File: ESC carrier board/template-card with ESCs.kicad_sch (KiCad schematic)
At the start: 13 parts, among them J1 Conn_01x10_Pin, J3 Conn_01x04_Pin, J4 Conn_01x04_Pin, J5 Conn_01x04_Pin, SW1 SW_DPDT_x2, U2 ESC, U4 ESC, U6 ESC

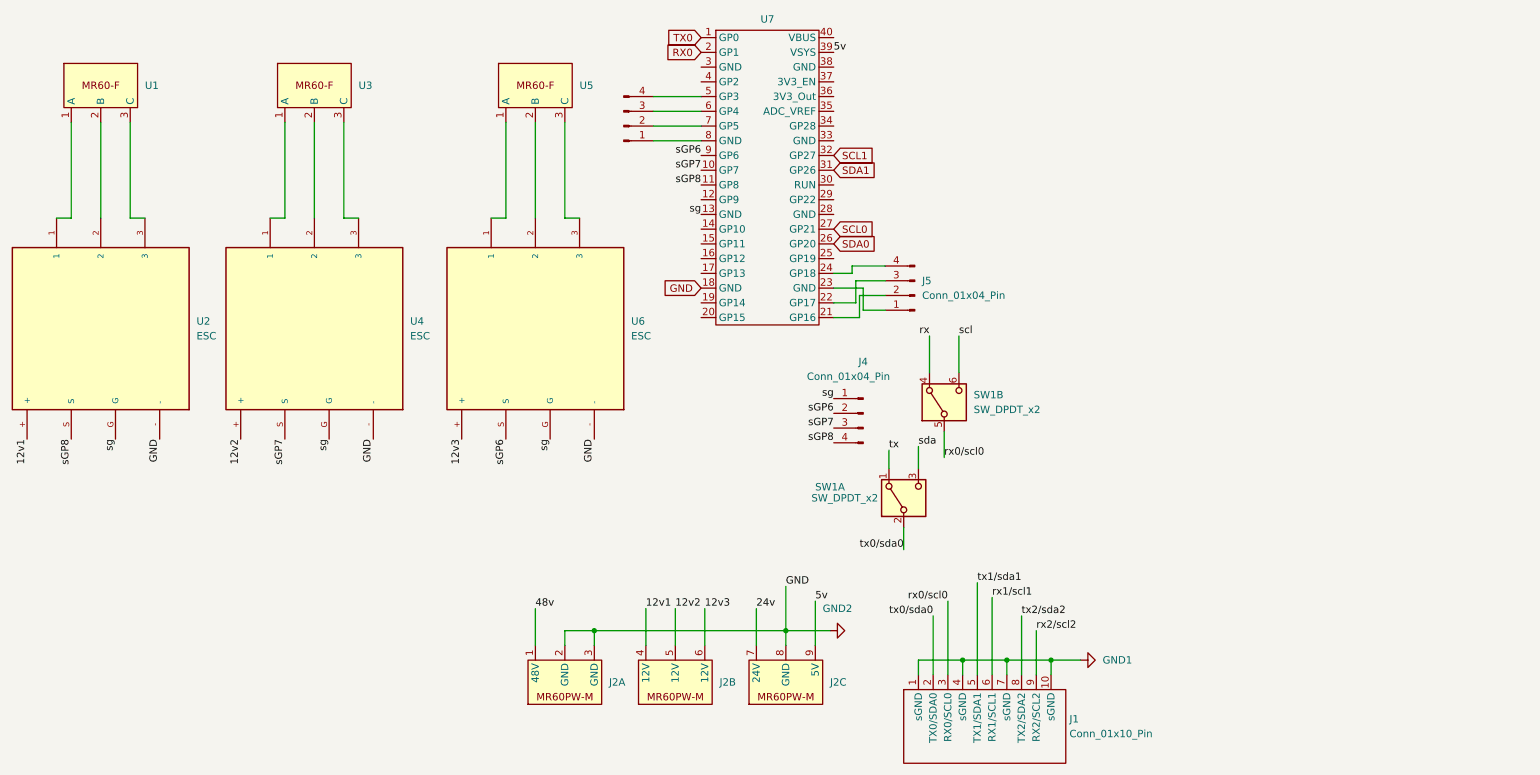
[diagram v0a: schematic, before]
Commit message: Routed board
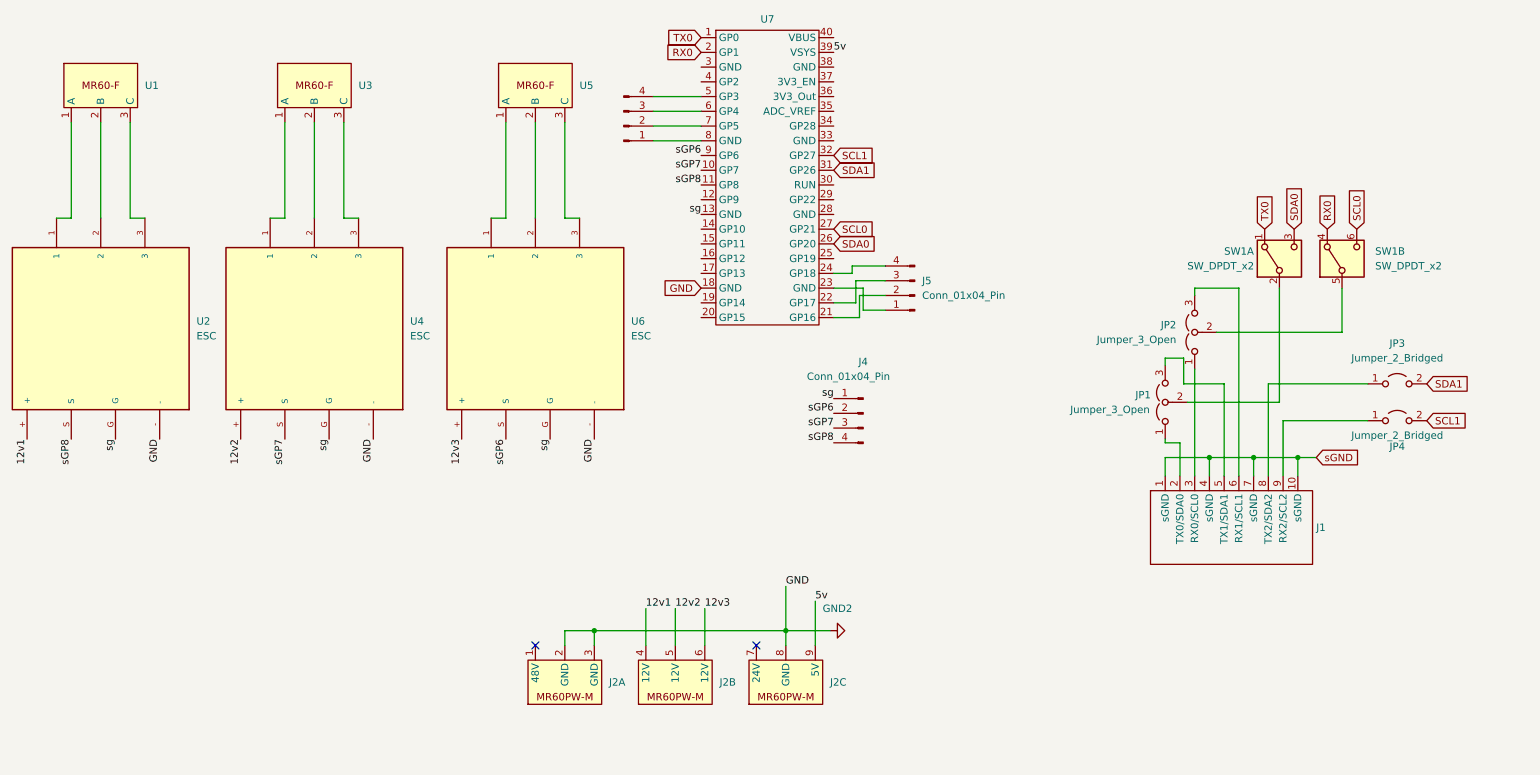
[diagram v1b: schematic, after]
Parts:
- added JP1, JP2: Jumper_3_Open, Jumper:SolderJumper-3_P1.3mm_Open_RoundedPad1.0x1.5mm, symbol Jumper:Jumper_3_Open
- added JP3, JP4: Jumper_2_Bridged, Jumper:SolderJumper-2_P1.3mm_Open_RoundedPad1.0x1.5mm, symbol Jumper:Jumper_2_Open
- J1: value Conn_01x10_Pin -> ~
- SW1: footprint 2024-backplane:SW_CUI_DPDT -> Kelpie_Default:CUI-Switch-SMD
- U1, U3, U5: footprint ESC-Thruster:MR60-F -> 2024-backplane:MR60-F
- U7: footprint ESC-carrier:ESP32-S3-Pico -> Kelpie_Default:ESP32-S3-Pico
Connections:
- net rx is gone; now on net RX0: SW1.4 (A)
- net scl is gone; now on net SCL0: SW1.6 (C)
- net sda is gone; now on net SDA0: SW1.3 (C)
- net tx is gone; now on net TX0: SW1.1 (A)
- net SCL1: now also JP4.2 (B)
- net SDA1: now also JP3.2 (B)
- net 24v: no longer names the net of J2.7 (24V)
- net 48v: no longer names the net of J2.1 (48V)
- net GND1 renamed sGND
- net rx0/scl0: no longer names the net of J1.3 (RX0/SCL0)
- net rx0/scl0: now also JP2.1 (A); no longer SW1.5 (B)
- net rx1/scl1: no longer names the net of J1.6 (RX1/SCL1)
- net rx1/scl1: now also JP2.3 (B)
- net rx2/scl2: no longer names the net of J1.9 (RX2/SCL2)
- net rx2/scl2: now also JP4.1 (A)
- net tx0/sda0: no longer names the net of J1.2 (TX0/SDA0)
- net tx0/sda0: now also JP1.1 (A); no longer SW1.2 (B)
- net tx1/sda1: no longer names the net of J1.5 (TX1/SDA1)
- net tx1/sda1: now also JP1.3 (B)
- net tx2/sda2: no longer names the net of J1.8 (TX2/SDA2)
- net tx2/sda2: now also JP3.1 (A)
- new net: JP2.2 (C), SW1.5 (B)
- new net: JP1.2 (C), SW1.2 (B)
- no-connect marks 0 -> 2

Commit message: Modified board and footprints
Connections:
- net sg is gone; now on net sGND: J4.1 (Pin_1), U2.G, U4.G, U6.G, U7.13 (GND)
- net GND2: now also J2.10 (Mount)
- net sGND: now also J3.1 (Pin_1), J5.1 (Pin_1), U7.23 (GND), U7.28 (GND), U7.3 (GND), U7.33 (GND), U7.38 (GND), U7.8 (GND)
- no-connect marks 2 -> 18
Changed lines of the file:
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@@
   (junction (at 236.855 89.535) (diameter 0) (color 0 0 0 0)
   )
+  (junction (at 172.085 64.135) (diameter 0) (color 0 0 0 0)
+  )
+  (junction (at 134.62 34.925) (diameter 0) (color 0 0 0 0)
+  )
   (junction (at 244.475 89.535) (diameter 0) (color 0 0 0 0)
   )
   (junction (at 156.21 119.38) (diameter 0) (color 0 0 0 0)
   )
+  (junction (at 139.7 47.625) (diameter 0) (color 0 0 0 0)
+  )
   (junction (at 123.19 119.38) (diameter 0) (color 0 0 0 0)
   )
   (junction (at 229.235 89.535) (diameter 0) (color 0 0 0 0)
   )
+  (no_connect (at 164.465 29.845))
+  (no_connect (at 141.605 57.785))
+  (no_connect (at 141.605 55.245))
+  (no_connect (at 164.465 55.245))
   (no_connect (at 151.13 121.92))
+  (no_connect (at 164.465 42.545))
+  (no_connect (at 164.465 17.145))
+  (no_connect (at 141.605 65.405))
+  (no_connect (at 164.465 27.305))
+  (no_connect (at 164.465 32.385))
+  (no_connect (at 164.465 45.085))
+  (no_connect (at 141.605 45.085))
+  (no_connect (at 164.465 24.765))
+  (no_connect (at 141.605 52.705))
+  (no_connect (at 141.605 62.865))
+  (no_connect (at 141.605 24.765))
   (no_connect (at 113.03 121.92))
+  (no_connect (at 141.605 50.165))
   (wire (pts (xy 80.01 48.26) (xy 80.01 31.75))
     (stroke (width 0) (type default))
   )
+  (wire (pts (xy 106.68 132.715) (xy 106.68 129.54))
+    (stroke (width 0) (type default))
+  )
   (wire (pts (xy 43.18 31.75) (xy 43.18 48.26))
     (stroke (width 0) (type default))
@@
     (stroke (width 0) (type default))
   )
+  (wire (pts (xy 139.7 47.625) (xy 139.7 50.165))
+    (stroke (width 0) (type default))
+  )
   (wire (pts (xy 167.64 57.785) (xy 167.64 56.515))
     (stroke (width 0) (type default))
@@
     (stroke (width 0) (type default))
   )
+  (wire (pts (xy 134.62 37.465) (xy 133.35 37.465))
+    (stroke (width 0) (type default))
+  )
   (wire (pts (xy 156.21 111.76) (xy 156.21 119.38))
     (stroke (width 0) (type default))
@@
     (stroke (width 0) (type default))
   )
+  (wire (pts (xy 139.7 47.625) (xy 141.605 47.625))
+    (stroke (width 0) (type default))
+  )
   (wire (pts (xy 133.35 29.845) (xy 141.605 29.845))
     (stroke (width 0) (type default))
@@
     (stroke (width 0) (type default))
   )
-  (wire (pts (xy 133.35 34.925) (xy 141.605 34.925))
+  (wire (pts (xy 133.35 34.925) (xy 134.62 34.925))
     (stroke (width 0) (type default))
   )
@@
     (stroke (width 0) (type default))
   )
+  (wire (pts (xy 106.68 129.54) (xy 109.22 129.54))
+    (stroke (width 0) (type default))
+  )
   (wire (pts (xy 241.935 83.185) (xy 256.54 83.185))
     (stroke (width 0) (type default))
@@
     (stroke (width 0) (type default))
   )
+  (wire (pts (xy 134.62 34.925) (xy 134.62 37.465))
+    (stroke (width 0) (type default))
+  )
   (wire (pts (xy 224.155 86.995) (xy 224.155 92.71))
     (stroke (width 0) (type default))
@@
     (stroke (width 0) (type default))
   )
+  (wire (pts (xy 172.085 64.135) (xy 172.085 67.31))
+    (stroke (width 0) (type default))
+  )
+  (wire (pts (xy 137.795 50.165) (xy 139.7 50.165))
+    (stroke (width 0) (type default))
+  )
   (wire (pts (xy 133.35 32.385) (xy 141.605 32.385))
     (stroke (width 0) (type default))
@@
     (stroke (width 0) (type default))
   )
-  (wire (pts (xy 169.545 64.135) (xy 173.355 64.135))
+  (wire (pts (xy 169.545 64.135) (xy 172.085 64.135))
     (stroke (width 0) (type default))
   )
@@
     (stroke (width 0) (type default))
   )
+  (wire (pts (xy 172.085 67.31) (xy 174.625 67.31))
+    (stroke (width 0) (type default))
+  )
   (wire (pts (xy 221.615 72.39) (xy 224.79 72.39))
     (stroke (width 0) (type default))
@@
     (stroke (width 0) (type default))
   )
+  (wire (pts (xy 172.085 64.135) (xy 173.355 64.135))
+    (stroke (width 0) (type default))
+  )
   (wire (pts (xy 38.1 31.75) (xy 38.1 48.26))
     (stroke (width 0) (type default))
@@
     (stroke (width 0) (type default))
   )
+  (wire (pts (xy 134.62 34.925) (xy 141.605 34.925))
+    (stroke (width 0) (type default))
+  )
   (wire (pts (xy 244.475 89.535) (xy 244.475 92.71))
     (stroke (width 0) (type default))
@@
   )
   (wire (pts (xy 241.935 92.71) (xy 241.935 83.185))
+    (stroke (width 0) (type default))
+  )
+  (wire (pts (xy 137.795 47.625) (xy 139.7 47.625))
     (stroke (width 0) (type default))
   )
@@
     (effects (font (size 1.27 1.27)) (justify right bottom))
   )
-  (label "sg" (at 141.605 47.625 180) (fields_autoplaced)
+  (label "sg" (at 137.795 47.625 180) (fields_autoplaced)
     (effects (font (size 1.27 1.27)) (justify right bottom))
   )
@@
     )
   )
+  (global_label "sGND" (shape input) (at 164.465 47.625 0) (fields_autoplaced)
+    (effects (font (size 1.27 1.27)) (justify left))
+    (property "Intersheetrefs" "${INTERSHEET_REFS}" (at 172.3488 47.625 0)
+      (effects (font (size 1.27 1.27)) (justify left) hide)
+    )
+  )
   (global_label "SDA1" (shape input) (at 266.7 76.835 0) (fields_autoplaced)
     (effects (font (size 1.27 1.27)) (justify left))
@@
     )
   )
+  (global_label "sGND" (shape input) (at 164.465 34.925 0) (fields_autoplaced)
+    (effects (font (size 1.27 1.27)) (justify left))
+    (property "Intersheetrefs" "${INTERSHEET_REFS}" (at 172.3488 34.925 0)
+      (effects (font (size 1.27 1.27)) (justify left) hide)
+    )
+  )
   (global_label "sGND" (shape input) (at 247.65 89.535 0) (fields_autoplaced)
     (effects (font (size 1.27 1.27)) (justify left))
@@
     )
   )
+  (global_label "sGND" (shape input) (at 141.605 22.225 180) (fields_autoplaced)
+    (effects (font (size 1.27 1.27)) (justify right))
+    (property "Intersheetrefs" "${INTERSHEET_REFS}" (at 133.7212 22.225 0)
+      (effects (font (size 1.27 1.27)) (justify right) hide)
+    )
+  )
+  (global_label "sGND" (shape input) (at 164.465 22.225 0) (fields_autoplaced)
+    (effects (font (size 1.27 1.27)) (justify left))
+    (property "Intersheetrefs" "${INTERSHEET_REFS}" (at 172.3488 22.225 0)
+      (effects (font (size 1.27 1.27)) (justify left) hide)
+    )
+  )
   (global_label "SDA1" (shape input) (at 164.465 40.005 0) (fields_autoplaced)
     (effects (font (size 1.27 1.27)) (justify left))
@@
     (effects (font (size 1.27 1.27)) (justify left))
     (property "Intersheetrefs" "${INTERSHEET_REFS}" (at 243.84 42.4022 90)
+      (effects (font (size 1.27 1.27)) (justify left) hide)
+    )
+  )
+  (global_label "sGND" (shape input) (at 174.625 67.31 0) (fields_autoplaced)
+    (effects (font (size 1.27 1.27)) (justify left))
+    (property "Intersheetrefs" "${INTERSHEET_REFS}" (at 182.5088 67.31 0)
       (effects (font (size 1.27 1.27)) (justify left) hide)
     )
@@
     (effects (font (size 1.27 1.27)) (justify right))
     (property "Intersheetrefs" "${INTERSHEET_REFS}" (at 134.9308 19.685 0)
+      (effects (font (size 1.27 1.27)) (justify right) hide)
+    )
+  )
+  (global_label "sGND" (shape input) (at 137.795 50.165 180) (fields_autoplaced)
+    (effects (font (size 1.27 1.27)) (justify right))
+    (property "Intersheetrefs" "${INTERSHEET_REFS}" (at 129.9112 50.165 0)
+      (effects (font (size 1.27 1.27)) (justify right) hide)
+    )
+  )
+  (global_label "sGND" (shape input) (at 133.35 37.465 180) (fields_autoplaced)
+    (effects (font (size 1.27 1.27)) (justify right))
+    (property "Intersheetrefs" "${INTERSHEET_REFS}" (at 125.4662 37.465 0)
       (effects (font (size 1.27 1.27)) (justify right) hide)
     )
@@
     )
   )
-  (symbol (lib_name "MR60PW-M_X3_1") (lib_id "2024-backplane:MR60PW-M_X3") (at 121.92 121.92 0) (mirror x) (unit 1)
+  (symbol (lib_id "power:GND2") (at 106.68 132.715 0) (unit 1)
+    (in_bom yes) (on_board yes) (dnp no)
+    (property "Reference" "#PWR01" (at 106.68 139.065 0)
+      (effects (font (size 1.27 1.27)) hide)
+    )
+    (property "Value" "GND2" (at 110.49 131.445 90)
+      (effects (font (size 1.27 1.27)) (justify right))
+    )
+    (property "Footprint" "" (at 106.68 132.715 0)
+      (effects (font (size 1.27 1.27)) hide)
+    )
+    (property "Datasheet" "" (at 106.68 132.715 0)
+      (effects (font (size 1.27 1.27)) hide)
+    )
+    (pin "1")
+    (instances
+      (project "template-card with ESCs"
+        (path "/447f7668-e44a-4076-b3cb-4e0f6120b53c"
+          (reference "#PWR01") (unit 1)
+        )
+      )
+    )
+  )
+  (symbol (lib_id "2024-backplane:MR60PW-M_X3") (at 121.92 121.92 0) (mirror x) (unit 1)
     (in_bom yes) (on_board yes) (dnp no) (fields_autoplaced)
     (property "Reference" "J2" (at 125.73 128.27 0)
@@
     (pin "5")
     (pin "3")
+    (pin "10")
     (instances
       (project "template-card with ESCs"
@@
     (pin "5")
     (pin "3")
+    (pin "10")
     (instances
       (project "template-card with ESCs"
@@
     (pin "5")
     (pin "3")
-    (instances
-      (project "template-card with ESCs"
+    (pin "10")
+    (instances
+      (project "template-card with ESCs"

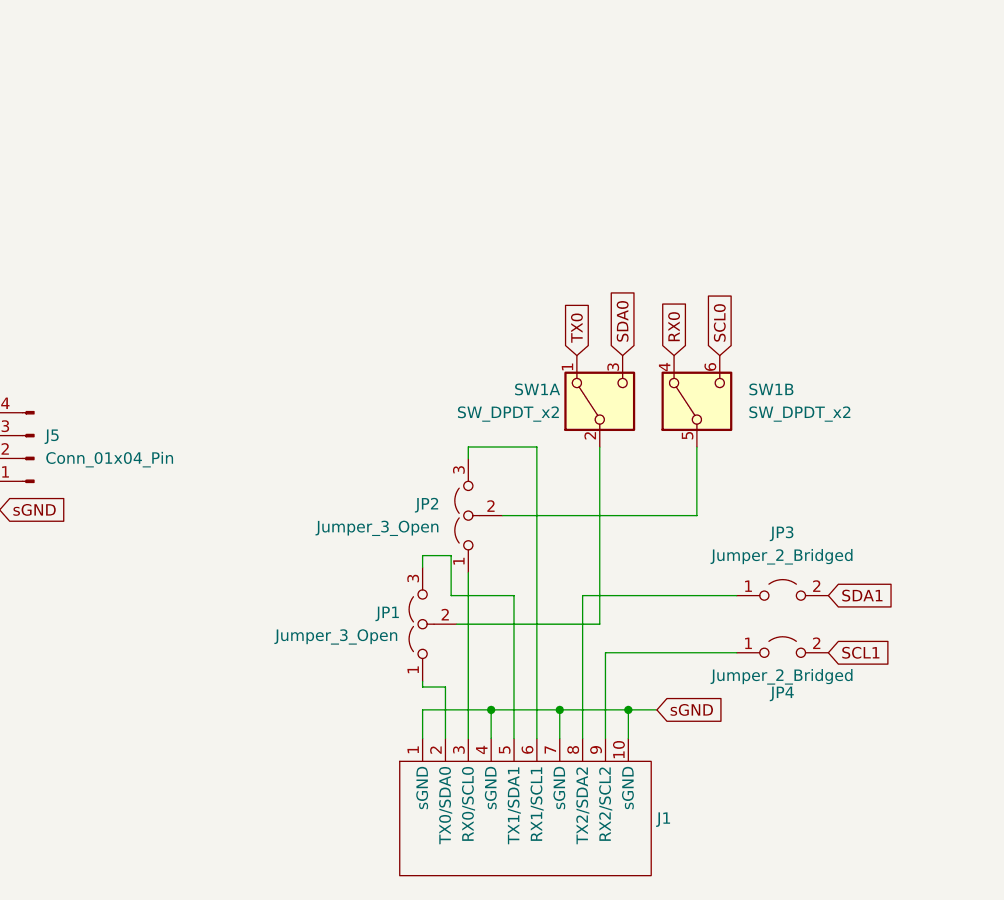
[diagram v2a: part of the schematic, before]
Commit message: ESC carrier board jumper routing
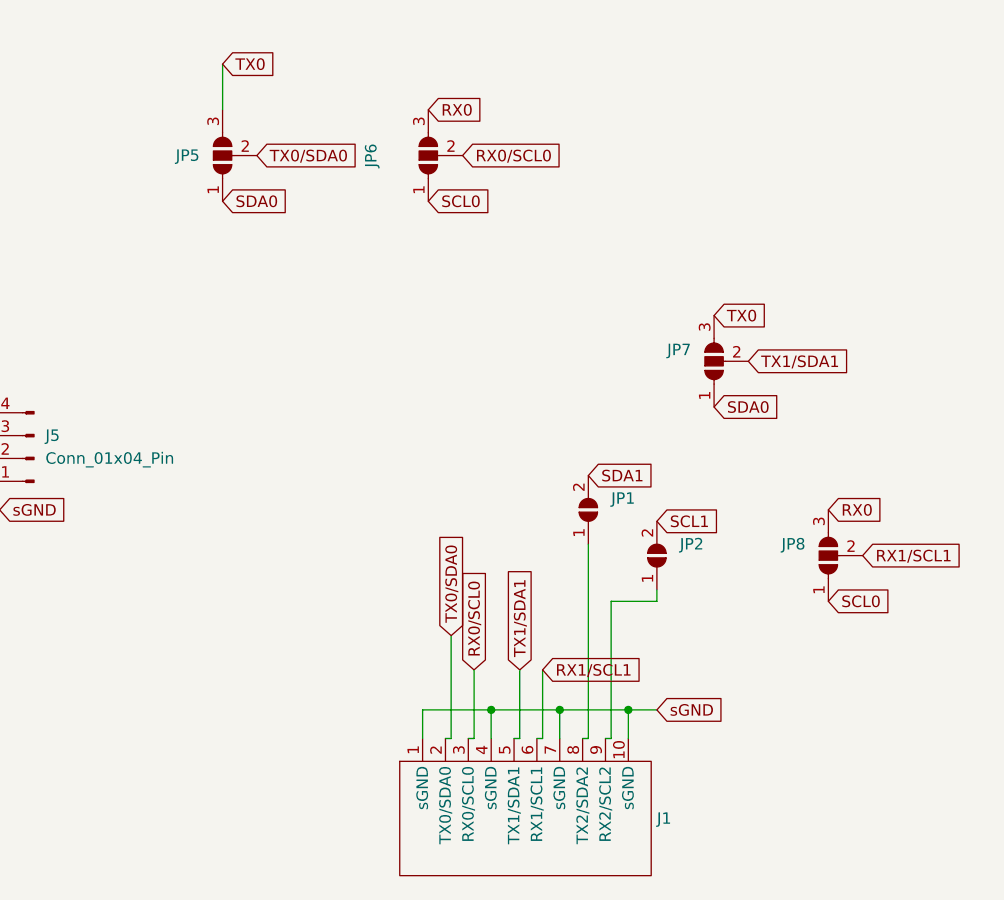
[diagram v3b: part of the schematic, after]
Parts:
- removed JP1, JP2: Jumper_3_Open, Jumper:SolderJumper-3_P1.3mm_Open_RoundedPad1.0x1.5mm, symbol Jumper:Jumper_3_Open
- removed JP3, JP4: Jumper_2_Bridged, Jumper:SolderJumper-2_P1.3mm_Open_RoundedPad1.0x1.5mm, symbol Jumper:Jumper_2_Open
- removed SW1: SW_DPDT_x2, Kelpie_Default:CUI-Switch-SMD, symbol Switch:SW_DPDT_x2
- added JP1, JP2: SolderJumper_2_Open, Jumper:SolderJumper-2_P1.3mm_Open_Pad1.0x1.5mm, symbol Jumper:SolderJumper_2_Open
- added JP5, JP6, JP7, JP8: SolderJumper_3_Open, Jumper:SolderJumper-3_P2.0mm_Open_TrianglePad1.0x1.5mm, symbol Jumper:SolderJumper_3_Open
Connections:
- net RX0: now also JP6.3 (B), JP8.3 (B)
- net SCL0: now also JP6.1 (A), JP8.1 (A)
- net SCL1: now also JP2.2 (B)
- net SDA0: now also JP5.1 (A), JP7.1 (A)
- net SDA1: now also JP1.2 (B)
- net TX0: now also JP5.3 (B), JP7.3 (B)
- net TX0/SDA0: now reaches J1.2 (TX0/SDA0)
- net TX0/SDA0: now also JP5.2 (C)
- net RX0/SCL0: now reaches J1.3 (RX0/SCL0)
- net RX0/SCL0: now also JP6.2 (C)
- net TX1/SDA1: now reaches J1.5 (TX1/SDA1)
- net TX1/SDA1: now also JP7.2 (C)
- net RX1/SCL1: now reaches J1.6 (RX1/SCL1)
- net RX1/SCL1: now also JP8.2 (C)
- net at J1.8 (TX2/SDA2): now also JP1.1 (A)
- net at J1.9 (RX2/SCL2): now also JP2.1 (A)
